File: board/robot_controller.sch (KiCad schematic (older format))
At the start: 56 parts, among them U2 STM32F405-144

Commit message: Reorganized schematic
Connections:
- net LED Data 0/DATA_OUT renamed LED Data 1/DATA_OUT
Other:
- note added: "24V ADC"
- note added: "3.3V Regulator"
- note removed: "Stepper Motor Driver Sense"
- moved on the sheet: C?, D?, J?, L?, R?, U?, UEXT0, UEXT1

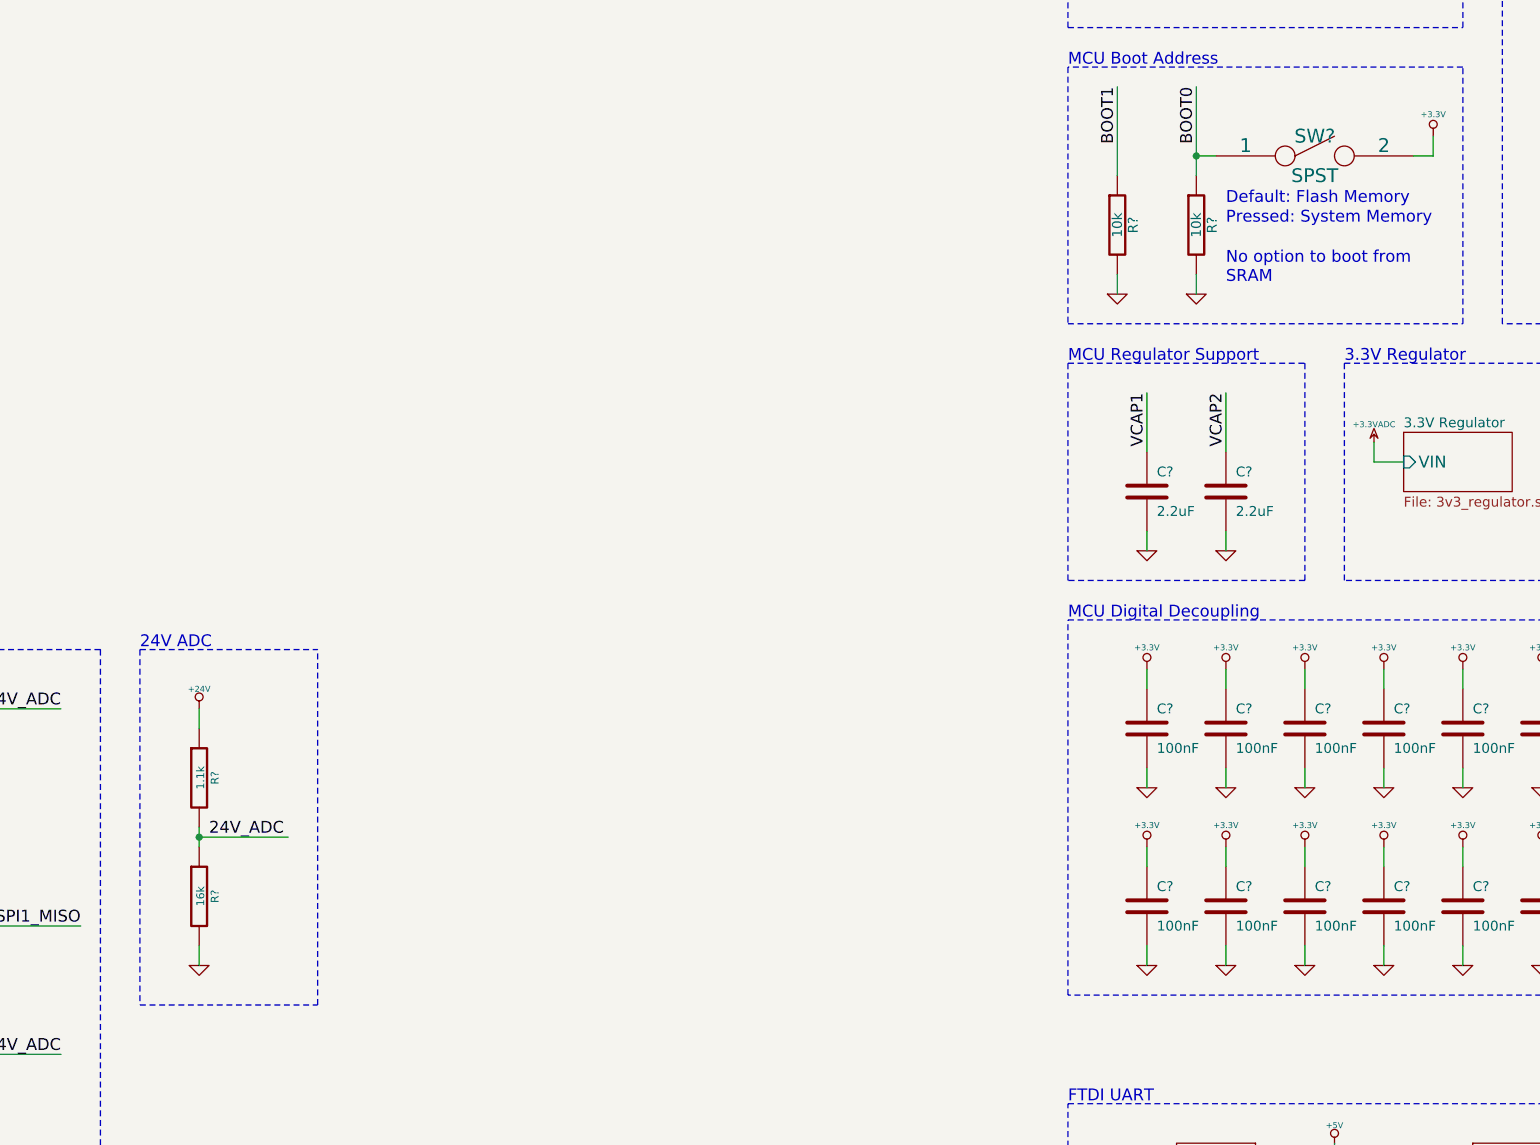
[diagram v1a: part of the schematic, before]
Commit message: Added 24V connector and fixed a few things on the 24V rail.
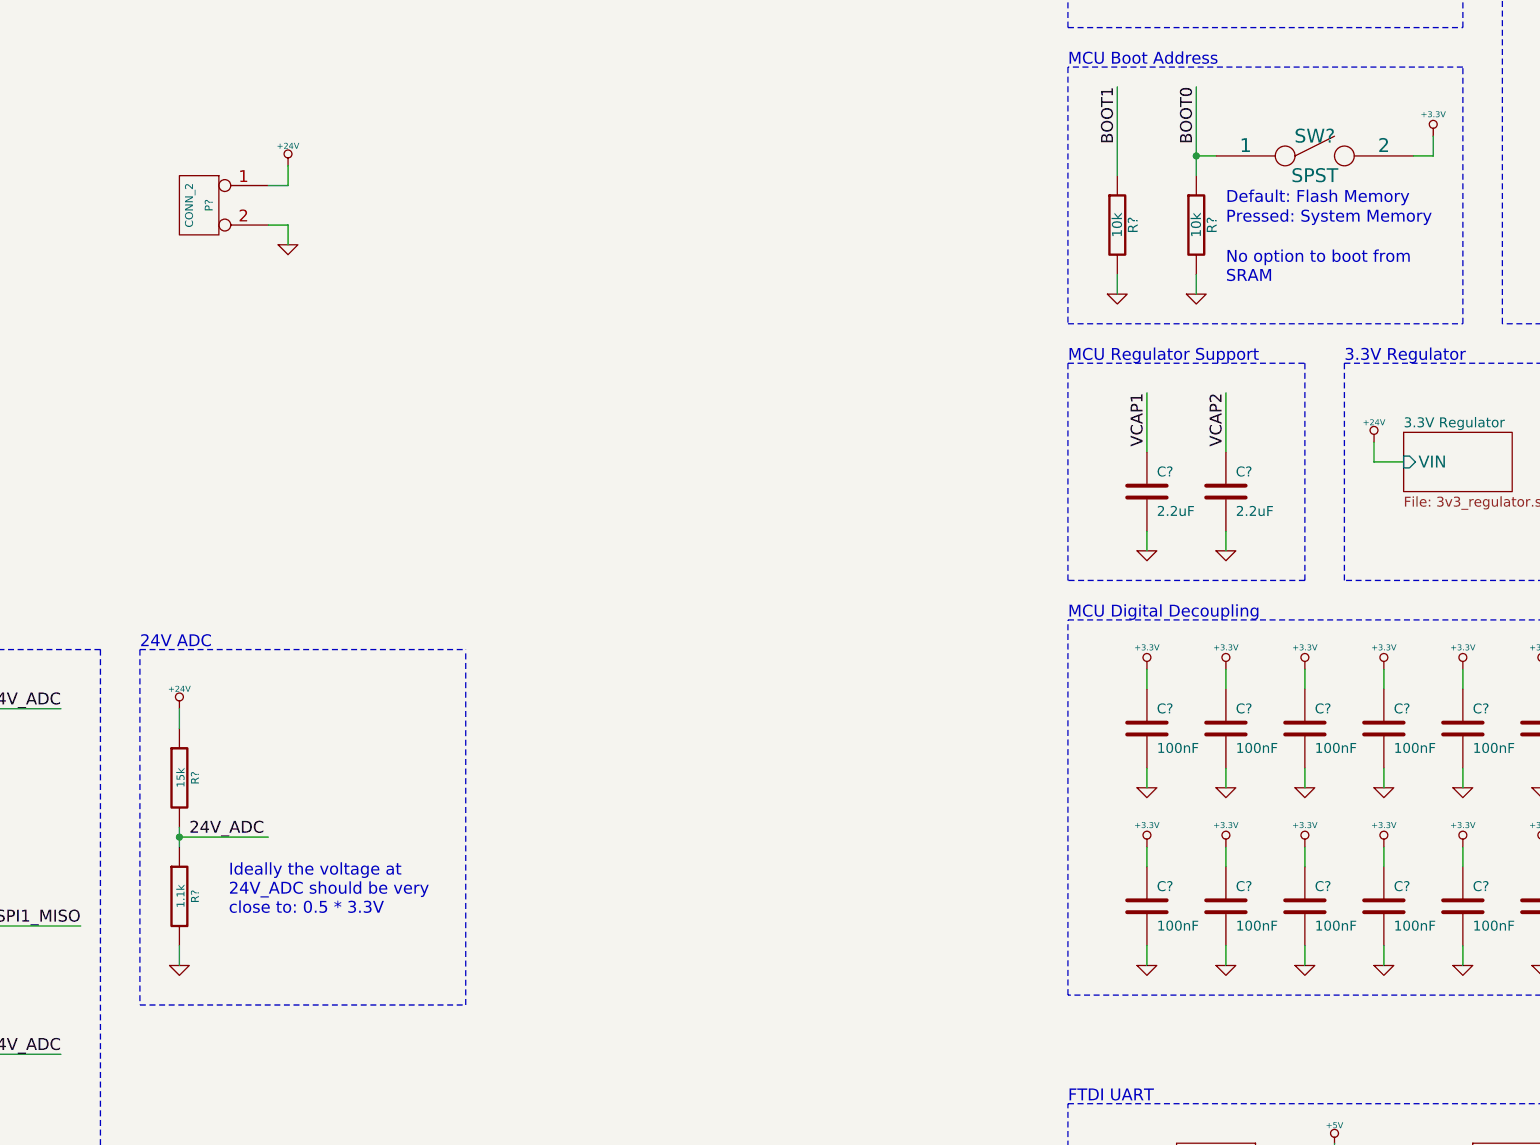
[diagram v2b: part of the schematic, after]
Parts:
- added P?: CONN_2, symbol CONN_2
- R?: value 1.1k -> 15k
- R?: value 16k -> 1.1k
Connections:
- net +24V: now also P?.1 (P1)
- net GND: now also P?.2 (PM)
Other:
- note added: "Ideally the voltage at\n24V_ADC should be very\nclose to: 0.5 * 3.3V"
- moved on the sheet: R?
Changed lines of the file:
@@
 L R R?
 U 1 1 52E86082
-P 25250 18700
-F 0 "R?" V 25330 18700 40  0000 C CNN
-F 1 "1.1k" V 25257 18701 40  0000 C CNN
-F 2 "" V 25180 18700 30  0000 C CNN
-F 3 "" H 25250 18700 30  0000 C CNN
-	1    25250 18700
+P 25150 18700
+F 0 "R?" V 25230 18700 40  0000 C CNN
+F 1 "15k" V 25157 18701 40  0000 C CNN
+F 2 "" V 25080 18700 30  0000 C CNN
+F 3 "" H 25150 18700 30  0000 C CNN
+	1    25150 18700
 	1    0    0    -1
 $EndComp
@@
 L R R?
 U 1 1 52E86096
-P 25250 19300
-F 0 "R?" V 25330 19300 40  0000 C CNN
-F 1 "16k" V 25257 19301 40  0000 C CNN
-F 2 "" V 25180 19300 30  0000 C CNN
-F 3 "" H 25250 19300 30  0000 C CNN
-	1    25250 19300
+P 25150 19300
+F 0 "R?" V 25230 19300 40  0000 C CNN
+F 1 "1.1k" V 25157 19301 40  0000 C CNN
+F 2 "" V 25080 19300 30  0000 C CNN
+F 3 "" H 25150 19300 30  0000 C CNN
+	1    25150 19300
 	1    0    0    -1
 $EndComp
@@
 L GND #PWR?
 U 1 1 52E865EF
-P 25250 19650
-F 0 "#PWR?" H 25250 19650 30  0001 C CNN
-F 1 "GND" H 25250 19580 30  0001 C CNN
-F 2 "" H 25250 19650 60  0000 C CNN
-F 3 "" H 25250 19650 60  0000 C CNN
-	1    25250 19650
+P 25150 19650
+F 0 "#PWR?" H 25150 19650 30  0001 C CNN
+F 1 "GND" H 25150 19580 30  0001 C CNN
+F 2 "" H 25150 19650 60  0000 C CNN
+F 3 "" H 25150 19650 60  0000 C CNN
+	1    25150 19650
 	1    0    0    -1
 $EndComp
@@
 L +24V #PWR?
 U 1 1 52E8699F
-P 25250 18350
-F 0 "#PWR?" H 25250 18300 20  0001 C CNN
-F 1 "+24V" H 25250 18450 30  0000 C CNN
-F 2 "" H 25250 18350 60  0000 C CNN
-F 3 "" H 25250 18350 60  0000 C CNN
-	1    25250 18350
-	1    0    0    -1
-$EndComp
-Text Label 25300 19000 0    60   ~ 0
+P 25150 18350
+F 0 "#PWR?" H 25150 18300 20  0001 C CNN
+F 1 "+24V" H 25150 18450 30  0000 C CNN
+F 2 "" H 25150 18350 60  0000 C CNN
+F 3 "" H 25150 18350 60  0000 C CNN
+	1    25150 18350
+	1    0    0    -1
+$EndComp
+Text Label 25200 19000 0    60   ~ 0
 24V_ADC
 Text Label 19200 18350 0    60   ~ 0
@@
 	19200 19450 20250 19450
 Wire Wire Line
-	25250 18350 25250 18450
-Wire Wire Line
-	25250 18950 25250 19000
-Wire Wire Line
-	25250 19000 25250 19050
-Wire Wire Line
-	25250 19550 25250 19650
-Wire Wire Line
-	25700 19000 25250 19000
-Connection ~ 25250 19000
+	25150 18350 25150 18450
+Wire Wire Line
+	25150 18950 25150 19000
+Wire Wire Line
+	25150 19000 25150 19050
+Wire Wire Line
+	25150 19550 25150 19650
+Wire Wire Line
+	25600 19000 25150 19000
+Connection ~ 25150 19000
 Wire Wire Line
 	19200 18350 20250 18350
@@
 	24750 18050 19000 18050
 Wire Notes Line
-	24950 18050 25850 18050
+	24950 18050 26600 18050
 Wire Notes Line
 	24950 18050 24950 19850
 Wire Notes Line
-	24950 19850 25850 19850
-Wire Notes Line
-	25850 19850 25850 18050
+	24950 19850 26600 19850
+Wire Notes Line
+	26600 19850 26600 18050
 Wire Wire Line
 	36000 17550 35400 17550
@@
 Wire Wire Line
 	31200 17100 31350 17100
-$Comp
-L +3.3VADC #PWR?
-U 1 1 52F5C543
+Text Notes 31050 16600 0    60   ~ 0
+3.3V Regulator
+Wire Notes Line
+	31050 16600 32450 16600
+Wire Notes Line
+	32450 16600 32450 17700
+Wire Notes Line
+	32450 17700 31050 17700
+Wire Notes Line
+	31050 17700 31050 16600
+$Comp
+L CONN_2 P?
+U 1 1 52F70171
+P 25250 15800
+F 0 "P?" V 25200 15800 40  0000 C CNN
+F 1 "CONN_2" V 25300 15800 40  0000 C CNN
+F 2 "" H 25250 15800 60  0000 C CNN
+F 3 "" H 25250 15800 60  0000 C CNN
+	1    25250 15800
+	-1   0    0    -1
+$EndComp
+$Comp
+L GND #PWR?
+U 1 1 52F70A93
+P 25700 16000
+F 0 "#PWR?" H 25700 16000 30  0001 C CNN
+F 1 "GND" H 25700 15930 30  0001 C CNN
+F 2 "" H 25700 16000 60  0000 C CNN
+F 3 "" H 25700 16000 60  0000 C CNN
+	1    25700 16000
+	1    0    0    -1
+$EndComp
+Wire Wire Line
+	25700 15600 25700 15700
+Wire Wire Line
+	25700 15700 25600 15700
+Wire Wire Line
+	25600 15900 25700 15900
+Wire Wire Line
+	25700 15900 25700 16000
+$Comp
+L +24V #PWR?
+U 1 1 52F75202
 P 31200 17000
-F 0 "#PWR?" H 31200 17120 20  0001 C CNN
-F 1 "+3.3VADC" H 31200 17090 30  0000 C CNN
+F 0 "#PWR?" H 31200 16950 20  0001 C CNN
+F 1 "+24V" H 31200 17100 30  0000 C CNN
 F 2 "" H 31200 17000 60  0000 C CNN
 F 3 "" H 31200 17000 60  0000 C CNN
@@
 	1    0    0    -1
 $EndComp
-Text Notes 31050 16600 0    60   ~ 0
-3.3V Regulator
-Wire Notes Line
-	31050 16600 32450 16600
-Wire Notes Line
-	32450 16600 32450 17700
-Wire Notes Line
-	32450 17700 31050 17700
-Wire Notes Line
-	31050 17700 31050 16600
+$Comp
+L +24V #PWR?
+U 1 1 52F76574
+P 25700 15600
+F 0 "#PWR?" H 25700 15550 20  0001 C CNN
+F 1 "+24V" H 25700 15700 30  0000 C CNN
+F 2 "" H 25700 15600 60  0000 C CNN
+F 3 "" H 25700 15600 60  0000 C CNN
+	1    25700 15600
+	1    0    0    -1
+$EndComp
+Text Notes 25400 19400 0    60   ~ 0
+Ideally the voltage at\n24V_ADC should be very\nclose to: 0.5 * 3.3V
 $EndSCHEMATC
